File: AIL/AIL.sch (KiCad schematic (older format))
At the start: 30 parts, among them J1 Screw_Terminal_01x02, J2 Screw_Terminal_01x02, Q1 BC548, U1 TPL290

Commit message: review das placas
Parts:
- added H? (x4): NC, e-Power:MountingHole_3.2mm_M3_Pad_Via, symbol Mechanical:MountingHole_Pad
- added TP?: GND, e-Power:TestPoint_Pad_D1.0mm, symbol Connector:TestPoint
- added TP?: +20V, e-Power:TestPoint_Pad_D1.0mm, symbol Connector:TestPoint
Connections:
- net +20V: now also TP?.1
- net GND: now also TP?.1
- no-connect marks 0 -> 4
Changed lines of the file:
@@
 Wire Wire Line
 	6500 2150 6500 2300
+$Comp
+L Connector:TestPoint TP?
+U 1 1 5F2DBCEA
+P 7400 5400
+F 0 "TP?" H 7342 5426 50  0000 R CNN
+F 1 "GND" H 7342 5517 50  0000 R CNN
+F 2 "e-Power:TestPoint_Pad_D1.0mm" H 7600 5400 50  0001 C CNN
+F 3 "~" H 7600 5400 50  0001 C CNN
+	1    7400 5400
+	-1   0    0    1
+$EndComp
+Connection ~ 7400 5400
+$Comp
+L Connector:TestPoint TP?
+U 1 1 5F2DC33C
+P 7400 4900
+F 0 "TP?" H 7458 5018 50  0000 L CNN
+F 1 "+20V" H 7458 4927 50  0000 L CNN
+F 2 "e-Power:TestPoint_Pad_D1.0mm" H 7600 4900 50  0001 C CNN
+F 3 "~" H 7600 4900 50  0001 C CNN
+	1    7400 4900
+	1    0    0    -1
+$EndComp
+Connection ~ 7400 4900
+$Comp
+L Mechanical:MountingHole_Pad H?
+U 1 1 5F2DCAE7
+P 8000 4900
+F 0 "H?" H 7950 5100 50  0000 L CNN
+F 1 "NC" H 8100 4858 50  0001 L CNN
+F 2 "e-Power:MountingHole_3.2mm_M3_Pad_Via" H 8000 4900 50  0001 C CNN
+F 3 "~" H 8000 4900 50  0001 C CNN
+	1    8000 4900
+	1    0    0    -1
+$EndComp
+NoConn ~ 8000 5000
+$Comp
+L Mechanical:MountingHole_Pad H?
+U 1 1 5F2E02B0
+P 8200 4900
+F 0 "H?" H 8150 5100 50  0000 L CNN
+F 1 "NC" H 8300 4858 50  0001 L CNN
+F 2 "e-Power:MountingHole_3.2mm_M3_Pad_Via" H 8200 4900 50  0001 C CNN
+F 3 "~" H 8200 4900 50  0001 C CNN
+	1    8200 4900
+	1    0    0    -1
+$EndComp
+$Comp
+L Mechanical:MountingHole_Pad H?
+U 1 1 5F2E0AF2
+P 8400 4900
+F 0 "H?" H 8350 5100 50  0000 L CNN
+F 1 "NC" H 8500 4858 50  0001 L CNN
+F 2 "e-Power:MountingHole_3.2mm_M3_Pad_Via" H 8400 4900 50  0001 C CNN
+F 3 "~" H 8400 4900 50  0001 C CNN
+	1    8400 4900
+	1    0    0    -1
+$EndComp
+$Comp
+L Mechanical:MountingHole_Pad H?
+U 1 1 5F2E0CF8
+P 8600 4900
+F 0 "H?" H 8550 5100 50  0000 L CNN
+F 1 "NC" H 8700 4858 50  0001 L CNN
+F 2 "e-Power:MountingHole_3.2mm_M3_Pad_Via" H 8600 4900 50  0001 C CNN
+F 3 "~" H 8600 4900 50  0001 C CNN
+	1    8600 4900
+	1    0    0    -1
+$EndComp
+NoConn ~ 8200 5000
+NoConn ~ 8400 5000
+NoConn ~ 8600 5000
 $EndSCHEMATC

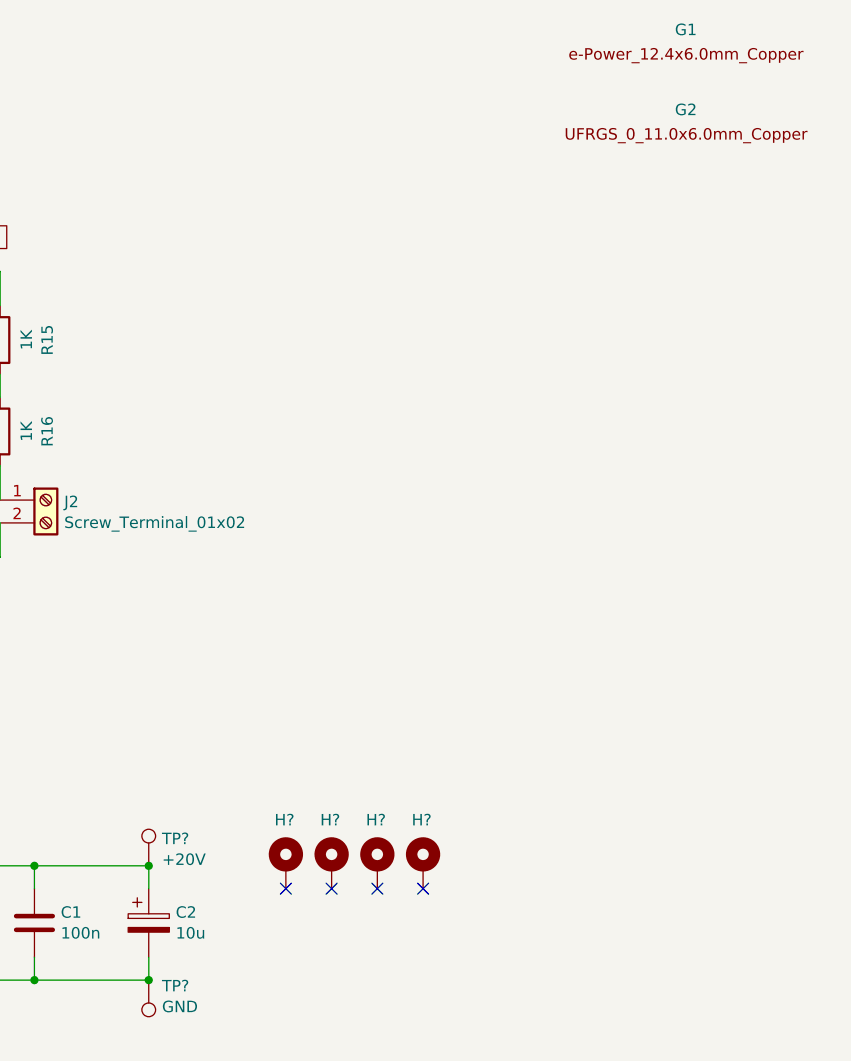
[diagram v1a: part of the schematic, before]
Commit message: AIL schematic and layout att. BSPD layout att.
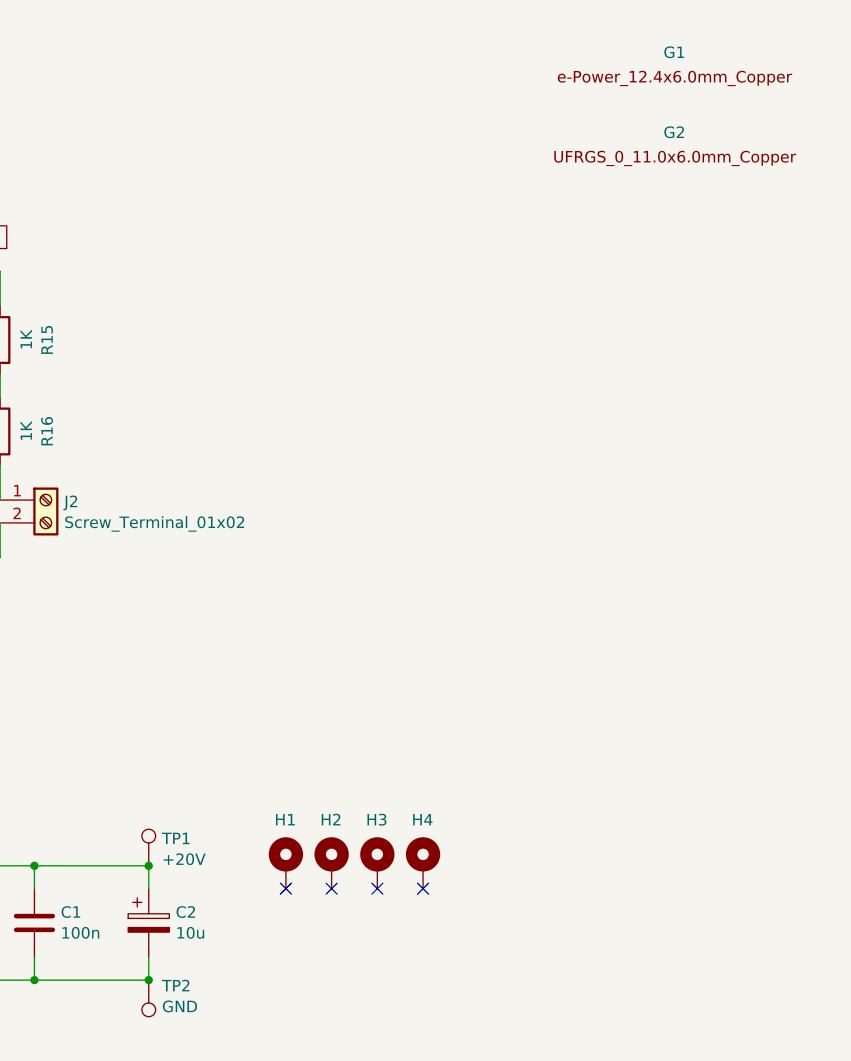
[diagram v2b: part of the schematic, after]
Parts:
- G1: footprint e-Power:e-Power_12.4x6.0mm_Copper -> e-Power:Logo_e-Power_12.4x6.0mm_SilkS
- G2: footprint e-Power:UFRGS_11.0x6.0mm_Copper -> e-Power:Logo_UFRGS_11.0x6.0mm_SilkS
- J1: footprint Connector_Phoenix_GMSTB:PhoenixContact_GMSTBA_2,5_2-G-7,62_1x02_P7.62mm_Horizontal -> e-Power:TerminalBlock_Phoenix_MKDS-1,5-2_1x02_P5.08mm_Horizontal
- J2: footprint Connector_PinHeader_2.54mm:PinHeader_1x02_P2.54mm_Horizontal -> e-Power:TerminalBlock_Phoenix_MKDS-1,5-2_1x02_P5.08mm_Horizontal
- gave numbers to parts that had none: 6
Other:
- moved on the sheet: G1, G2
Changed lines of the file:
@@
 F 0 "J1" H 3550 1800 50  0000 C CNN
 F 1 "Screw_Terminal_01x02" H 3468 1916 50  0001 C CNN
-F 2 "Connector_Phoenix_GMSTB:PhoenixContact_GMSTBA_2,5_2-G-7,62_1x02_P7.62mm_Horizontal" H 3550 2150 50  0001 C CNN
+F 2 "e-Power:TerminalBlock_Phoenix_MKDS-1,5-2_1x02_P5.08mm_Horizontal" H 3550 2150 50  0001 C CNN
 F 3 "~" H 3550 2150 50  0001 C CNN
 F 4 "Tractive System Voltage" H 3550 1900 50  0000 C CNN "Comment"
@@
 L e-Power:e-Power_12.4x6.0mm_Copper G1
 U 1 1 5E91CE08
-P 9750 1350
-F 0 "G1" H 9750 1457 50  0000 C CNN
-F 1 "e-Power_12.4x6.0mm_Copper" H 9750 1450 50  0001 C CNN
-F 2 "e-Power:e-Power_12.4x6.0mm_Copper" H 9750 1550 50  0001 C CNN
-F 3 "" H 9750 1350 50  0001 C CNN
-	1    9750 1350
+P 9700 1450
+F 0 "G1" H 9700 1557 50  0000 C CNN
+F 1 "e-Power_12.4x6.0mm_Copper" H 9700 1550 50  0001 C CNN
+F 2 "e-Power:Logo_e-Power_12.4x6.0mm_SilkS" H 9700 1650 50  0001 C CNN
+F 3 "" H 9700 1450 50  0001 C CNN
+	1    9700 1450
 	1    0    0    -1
 $EndComp
@@
 L e-Power:UFRGS_1_11.0x6.0mm_Copper G2
 U 1 1 5E9314EC
-P 9750 1700
-F 0 "G2" H 9750 1807 50  0000 C CNN
-F 1 "UFRGS_1_11.0x6.0mm_Copper" H 9750 1800 50  0001 C CNN
-F 2 "e-Power:UFRGS_11.0x6.0mm_Copper" H 9750 1900 50  0001 C CNN
-F 3 "" H 9750 1700 50  0001 C CNN
-	1    9750 1700
+P 9700 1800
+F 0 "G2" H 9700 1907 50  0000 C CNN
+F 1 "UFRGS_1_11.0x6.0mm_Copper" H 9700 1900 50  0001 C CNN
+F 2 "e-Power:Logo_UFRGS_11.0x6.0mm_SilkS" H 9700 2000 50  0001 C CNN
+F 3 "" H 9700 1800 50  0001 C CNN
+	1    9700 1800
 	1    0    0    -1
 $EndComp
@@
 F 0 "J2" H 7030 3292 50  0000 L CNN
 F 1 "Screw_Terminal_01x02" H 7030 3201 50  0000 L CNN
-F 2 "Connector_PinHeader_2.54mm:PinHeader_1x02_P2.54mm_Horizontal" H 6950 3300 50  0001 C CNN
+F 2 "e-Power:TerminalBlock_Phoenix_MKDS-1,5-2_1x02_P5.08mm_Horizontal" H 6950 3300 50  0001 C CNN
 F 3 "~" H 6950 3300 50  0001 C CNN
 	1    6950 3300
@@
 	6500 2150 6500 2300
 $Comp
-L Connector:TestPoint TP?
+L Connector:TestPoint TP2
 U 1 1 5F2DBCEA
 P 7400 5400
-F 0 "TP?" H 7342 5426 50  0000 R CNN
+F 0 "TP2" H 7342 5426 50  0000 R CNN
 F 1 "GND" H 7342 5517 50  0000 R CNN
 F 2 "e-Power:TestPoint_Pad_D1.0mm" H 7600 5400 50  0001 C CNN
@@
 Connection ~ 7400 5400
 $Comp
-L Connector:TestPoint TP?
+L Connector:TestPoint TP1
 U 1 1 5F2DC33C
 P 7400 4900
-F 0 "TP?" H 7458 5018 50  0000 L CNN
+F 0 "TP1" H 7458 5018 50  0000 L CNN
 F 1 "+20V" H 7458 4927 50  0000 L CNN
 F 2 "e-Power:TestPoint_Pad_D1.0mm" H 7600 4900 50  0001 C CNN
@@
 Connection ~ 7400 4900
 $Comp
-L Mechanical:MountingHole_Pad H?
+L Mechanical:MountingHole_Pad H1
 U 1 1 5F2DCAE7
 P 8000 4900
-F 0 "H?" H 7950 5100 50  0000 L CNN
+F 0 "H1" H 7950 5100 50  0000 L CNN
 F 1 "NC" H 8100 4858 50  0001 L CNN
 F 2 "e-Power:MountingHole_3.2mm_M3_Pad_Via" H 8000 4900 50  0001 C CNN
@@
 NoConn ~ 8000 5000
 $Comp
-L Mechanical:MountingHole_Pad H?
+L Mechanical:MountingHole_Pad H2
 U 1 1 5F2E02B0
 P 8200 4900
-F 0 "H?" H 8150 5100 50  0000 L CNN
+F 0 "H2" H 8150 5100 50  0000 L CNN
 F 1 "NC" H 8300 4858 50  0001 L CNN
 F 2 "e-Power:MountingHole_3.2mm_M3_Pad_Via" H 8200 4900 50  0001 C CNN
@@
 $EndComp
 $Comp
-L Mechanical:MountingHole_Pad H?
+L Mechanical:MountingHole_Pad H3
 U 1 1 5F2E0AF2
 P 8400 4900
-F 0 "H?" H 8350 5100 50  0000 L CNN
+F 0 "H3" H 8350 5100 50  0000 L CNN
 F 1 "NC" H 8500 4858 50  0001 L CNN
 F 2 "e-Power:MountingHole_3.2mm_M3_Pad_Via" H 8400 4900 50  0001 C CNN
@@
 $EndComp
 $Comp
-L Mechanical:MountingHole_Pad H?
+L Mechanical:MountingHole_Pad H4
 U 1 1 5F2E0CF8
 P 8600 4900
-F 0 "H?" H 8550 5100 50  0000 L CNN
+F 0 "H4" H 8550 5100 50  0000 L CNN
 F 1 "NC" H 8700 4858 50  0001 L CNN
 F 2 "e-Power:MountingHole_3.2mm_M3_Pad_Via" H 8600 4900 50  0001 C CNN

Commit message: att set/reset and ail 07/09/2020
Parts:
- removed G1: e-Power_12.4x6.0mm_Copper, e-Power:Logo_e-Power_12.4x6.0mm_SilkS, symbol e-Power:e-Power_12.4x6.0mm_Copper
- removed G2: UFRGS_1_11.0x6.0mm_Copper, e-Power:Logo_UFRGS_11.0x6.0mm_SilkS, symbol e-Power:UFRGS_1_11.0x6.0mm_Copper
- added G1: Logo_e-Power_Large, e-Power:Logo_e-Power_16.5x8.0mm_SilkS, symbol e-Power:Logo_e-Power_Large
- added G2: Logo_UFRGS_Large, e-Power:Logo_UFRGS_14.7x8.0mm_SilkS, symbol e-Power:Logo_UFRGS_Large
- C2: footprint e-Power:CP_Elec_10x10 -> Capacitor_SMD:CP_Elec_8x10
- D1, D2, D3: footprint e-Power:DO-41_SMD -> e-Power:DO-35_SMD
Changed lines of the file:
@@
 F 0 "D2" V 4563 3479 50  0000 L CNN
 F 1 "1N4747A" V 4654 3479 50  0000 L CNN
-F 2 "e-Power:DO-41_SMD" H 4700 3225 50  0001 C CNN
+F 2 "e-Power:DO-35_SMD" H 4700 3225 50  0001 C CNN
 F 3 "https://www.vishay.com/docs/85816/1n4728a.pdf" H 4700 3400 50  0001 C CNN
 F 4 "20V" V 4745 3479 50  0000 L CNN "Voltage"
@@
 F 0 "D1" V 4563 3079 50  0000 L CNN
 F 1 "1N4747A" V 4654 3079 50  0000 L CNN
-F 2 "e-Power:DO-41_SMD" H 4700 2825 50  0001 C CNN
+F 2 "e-Power:DO-35_SMD" H 4700 2825 50  0001 C CNN
 F 3 "https://www.vishay.com/docs/85816/1n4728a.pdf" H 4700 3000 50  0001 C CNN
 F 4 "20V" V 4745 3079 50  0000 L CNN "Voltage"
@@
 	4300 4050 4200 4050
 $Comp
-L e-Power:e-Power_12.4x6.0mm_Copper G1
-U 1 1 5E91CE08
-P 9700 1450
-F 0 "G1" H 9700 1557 50  0000 C CNN
-F 1 "e-Power_12.4x6.0mm_Copper" H 9700 1550 50  0001 C CNN
-F 2 "e-Power:Logo_e-Power_12.4x6.0mm_SilkS" H 9700 1650 50  0001 C CNN
-F 3 "" H 9700 1450 50  0001 C CNN
-	1    9700 1450
-	1    0    0    -1
-$EndComp
-$Comp
-L e-Power:UFRGS_1_11.0x6.0mm_Copper G2
-U 1 1 5E9314EC
-P 9700 1800
-F 0 "G2" H 9700 1907 50  0000 C CNN
-F 1 "UFRGS_1_11.0x6.0mm_Copper" H 9700 1900 50  0001 C CNN
-F 2 "e-Power:Logo_UFRGS_11.0x6.0mm_SilkS" H 9700 2000 50  0001 C CNN
-F 3 "" H 9700 1800 50  0001 C CNN
-	1    9700 1800
-	1    0    0    -1
-$EndComp
-$Comp
 L Isolator:SFH620A-1X006 U1
 U 1 1 5EEAFA46
@@
 F 0 "D3" V 6163 5229 50  0000 L CNN
 F 1 "1N4747A" V 6254 5229 50  0000 L CNN
-F 2 "e-Power:DO-41_SMD" H 6300 4975 50  0001 C CNN
+F 2 "e-Power:DO-35_SMD" H 6300 4975 50  0001 C CNN
 F 3 "https://www.vishay.com/docs/85816/1n4728a.pdf" H 6300 5150 50  0001 C CNN
 F 4 "20V" V 6345 5229 50  0000 L CNN "Voltage"
@@
 F 0 "C2" H 7518 5196 50  0000 L CNN
 F 1 "10u" H 7518 5105 50  0000 L CNN
-F 2 "e-Power:CP_Elec_10x10" H 7438 5000 50  0001 C CNN
+F 2 "Capacitor_SMD:CP_Elec_8x10" H 7438 5000 50  0001 C CNN
 F 3 "~" H 7400 5150 50  0001 C CNN
 	1    7400 5150
@@
 NoConn ~ 8400 5000
 NoConn ~ 8600 5000
+$Comp
+L e-Power:Logo_UFRGS_Large G2
+U 1 1 5F5590C7
+P 7900 2700
+F 0 "G2" H 7900 2500 60  0001 C CNN
+F 1 "Logo_UFRGS_Large" H 7900 2900 60  0001 C CNN
+F 2 "e-Power:Logo_UFRGS_14.7x8.0mm_SilkS" H 7900 2700 50  0001 C CNN
+F 3 "" H 7900 2700 50  0001 C CNN
+	1    7900 2700
+	1    0    0    -1
+$EndComp
+$Comp
+L e-Power:Logo_e-Power_Large G1
+U 1 1 5F559F30
+P 7900 2300
+F 0 "G1" H 7900 2125 60  0001 C CNN
+F 1 "Logo_e-Power_Large" H 7900 2500 60  0001 C CNN
+F 2 "e-Power:Logo_e-Power_16.5x8.0mm_SilkS" H 7900 2300 50  0001 C CNN
+F 3 "" H 7900 2300 50  0001 C CNN
+	1    7900 2300
+	1    0    0    -1
+$EndComp
 $EndSCHEMATC

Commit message: AIL atualizado
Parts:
- removed Q1: BC548, e-Power:SOT-23, symbol Transistor_BJT:BC548
- added Q1: BC807, Package_TO_SOT_SMD:SOT-23, symbol Transistor_BJT:BC807
- R5: value 10K -> 1K
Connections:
- net +20V: now also Q1.2 (E); no longer R13.1, R15.1
- net GND: now also D4.1 (K), J2.2 (Pin_2)
- net at R6.1: now also Q1.1 (B)
- new net: Q1.3 (C), R13.1, R15.1
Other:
- moved on the sheet: D1, D2, D4, F1, F2, J1, J2, R1, R13, R14, R15, R16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
